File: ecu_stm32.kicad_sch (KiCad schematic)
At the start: 46 parts, among them J16 USB-C, J17 ARM Cortex Debug, Y2 16MHz

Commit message: Finished
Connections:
- net MEM1_nCS: now also U40.59 (PF11); no longer U40.50 (PA4)
- net RADIO1_DIO0 renamed ECU_GS
- new net ECU_BV: U40.50 (PA4)
- no-connect marks 73 -> 72
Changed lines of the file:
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@@
 	)
 	(no_connect
-		(at 193.04 96.52)
-	)
-	(no_connect
 		(at 162.56 86.36)
 	)
@@
 		)
 	)
+	(global_label "ECU_GS"
+		(shape input)
+		(at 193.04 76.2 0)
+		(fields_autoplaced yes)
+		(effects
+			(font
+				(size 1.27 1.27)
+			)
+			(justify left)
+		)
+		(property "Intersheetrefs" "${INTERSHEET_REFS}"
+			(at 203.2218 76.2 0)
+			(effects
+				(font
+					(size 1.27 1.27)
+				)
+				(justify left)
+				(hide yes)
+			)
+		)
+	)
 	(global_label "IMU_MOSI"
 		(shape input)
@@
 		)
 	)
+	(global_label "ECU_BV"
+		(shape input)
+		(at 162.56 30.48 180)
+		(fields_autoplaced yes)
+		(effects
+			(font
+				(size 1.27 1.27)
+			)
+			(justify right)
+		)
+		(property "Intersheetrefs" "${INTERSHEET_REFS}"
+			(at 152.4991 30.48 0)
+			(effects
+				(font
+					(size 1.27 1.27)
+				)
+				(justify right)
+				(hide yes)
+			)
+		)
+	)
 	(global_label "PT4"
 		(shape input)
@@
 		)
 	)
-	(global_label "RADIO1_DIO0"
-		(shape input)
-		(at 193.04 76.2 0)
-		(fields_autoplaced yes)
-		(effects
-			(font
-				(size 1.27 1.27)
-			)
-			(justify left)
-		)
-		(property "Intersheetrefs" "${INTERSHEET_REFS}"
-			(at 208.181 76.2 0)
-			(effects
-				(font
-					(size 1.27 1.27)
-				)
-				(justify left)
-				(hide yes)
-			)
-		)
-	)
 	(global_label "GPS_INT"
 		(shape input)
@@
 		)
 	)
-	(global_label "MEM1_nCS"
+	(global_label "GPS_TX"
 		(shape input)
-		(at 162.56 30.48 180)
+		(at 162.56 22.86 180)
 		(fields_autoplaced yes)
 		(effects
@@
 		)
 		(property "Intersheetrefs" "${INTERSHEET_REFS}"
-			(at 149.7174 30.48 0)
+			(at 152.6806 22.86 0)
 			(effects
 				(font
@@
 		)
 	)
-	(global_label "GPS_TX"
+	(global_label "RADIO_MISO"
 		(shape input)
-		(at 162.56 22.86 180)
+		(at 193.04 88.9 0)
 		(fields_autoplaced yes)
 		(effects
@@
 				(size 1.27 1.27)
 			)
-			(justify right)
+			(justify left)
 		)
 		(property "Intersheetrefs" "${INTERSHEET_REFS}"
-			(at 152.6806 22.86 0)
+			(at 207.0735 88.9 0)
 			(effects
 				(font
 					(size 1.27 1.27)
 				)
-				(justify right)
+				(justify left)
 				(hide yes)
 			)
 		)
 	)
-	(global_label "RADIO_MISO"
+	(global_label "MEM1_nCS"
 		(shape input)
-		(at 193.04 88.9 0)
+		(at 193.04 96.52 0)
 		(fields_autoplaced yes)
 		(effects
@@
 		)
 		(property "Intersheetrefs" "${INTERSHEET_REFS}"
-			(at 207.0735 88.9 0)
+			(at 205.8826 96.52 0)
 			(effects
 				(font

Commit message: Fully up to date
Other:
- note added: "IN IOC PH1 is OSC OUT"
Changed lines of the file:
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@@
+		)
+	)
+	(text "IN IOC PH1 is OSC OUT"
+		(exclude_from_sim no)
+		(at 255.016 64.262 0)
+		(effects
+			(font
+				(size 1.27 1.27)
+			)
 		)
 	)

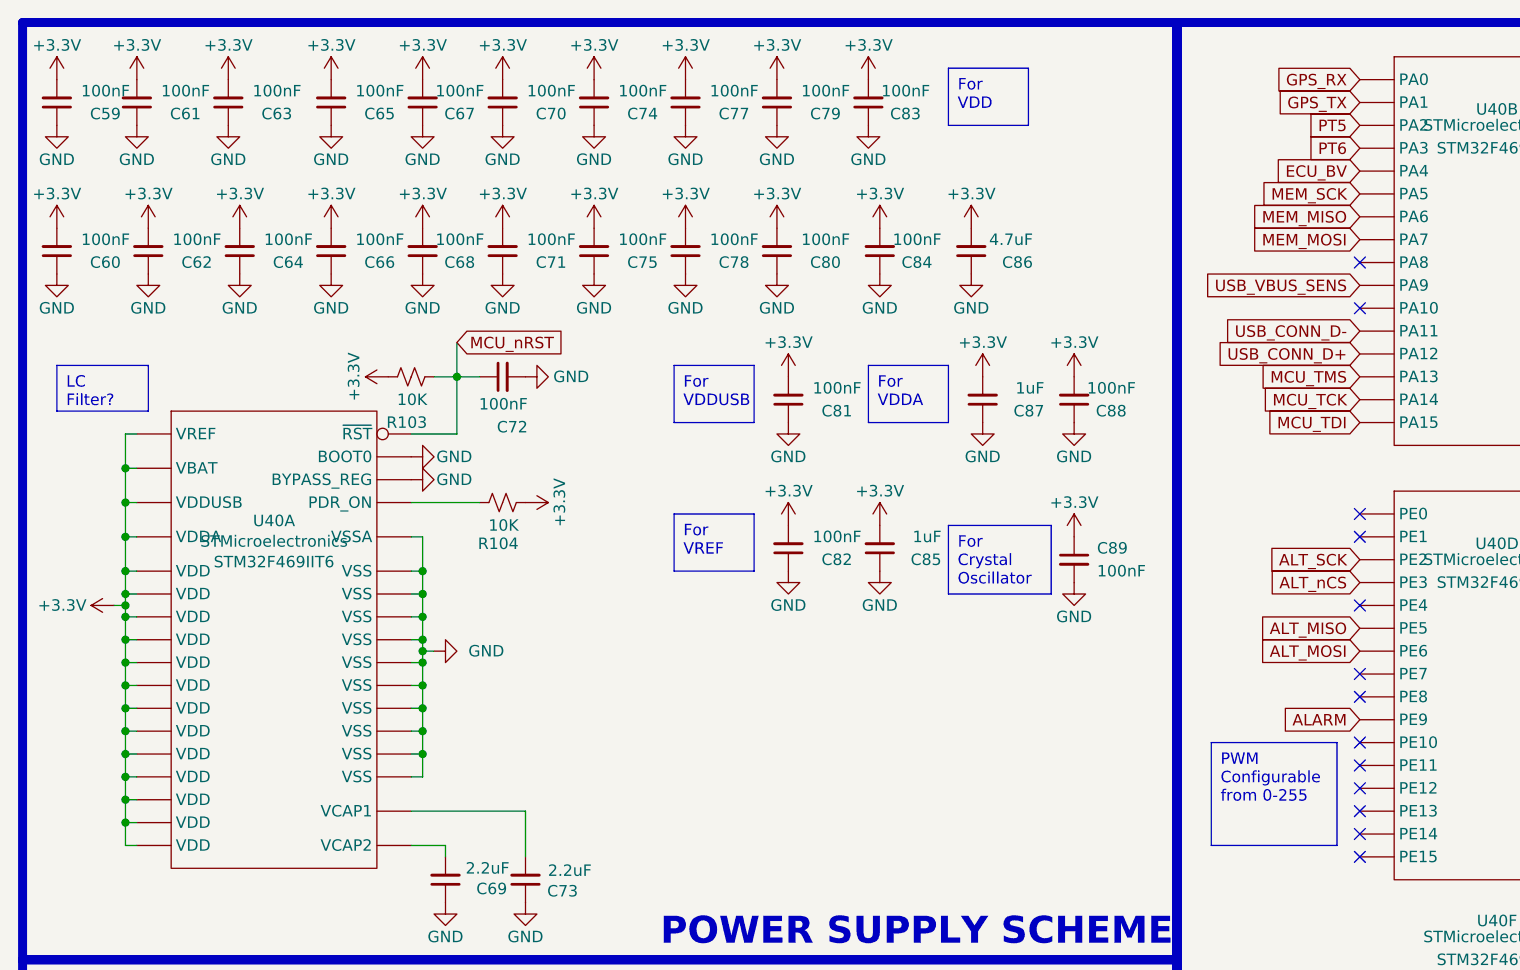
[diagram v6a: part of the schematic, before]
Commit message: REDS updated with diodes and hierarchy to main micro
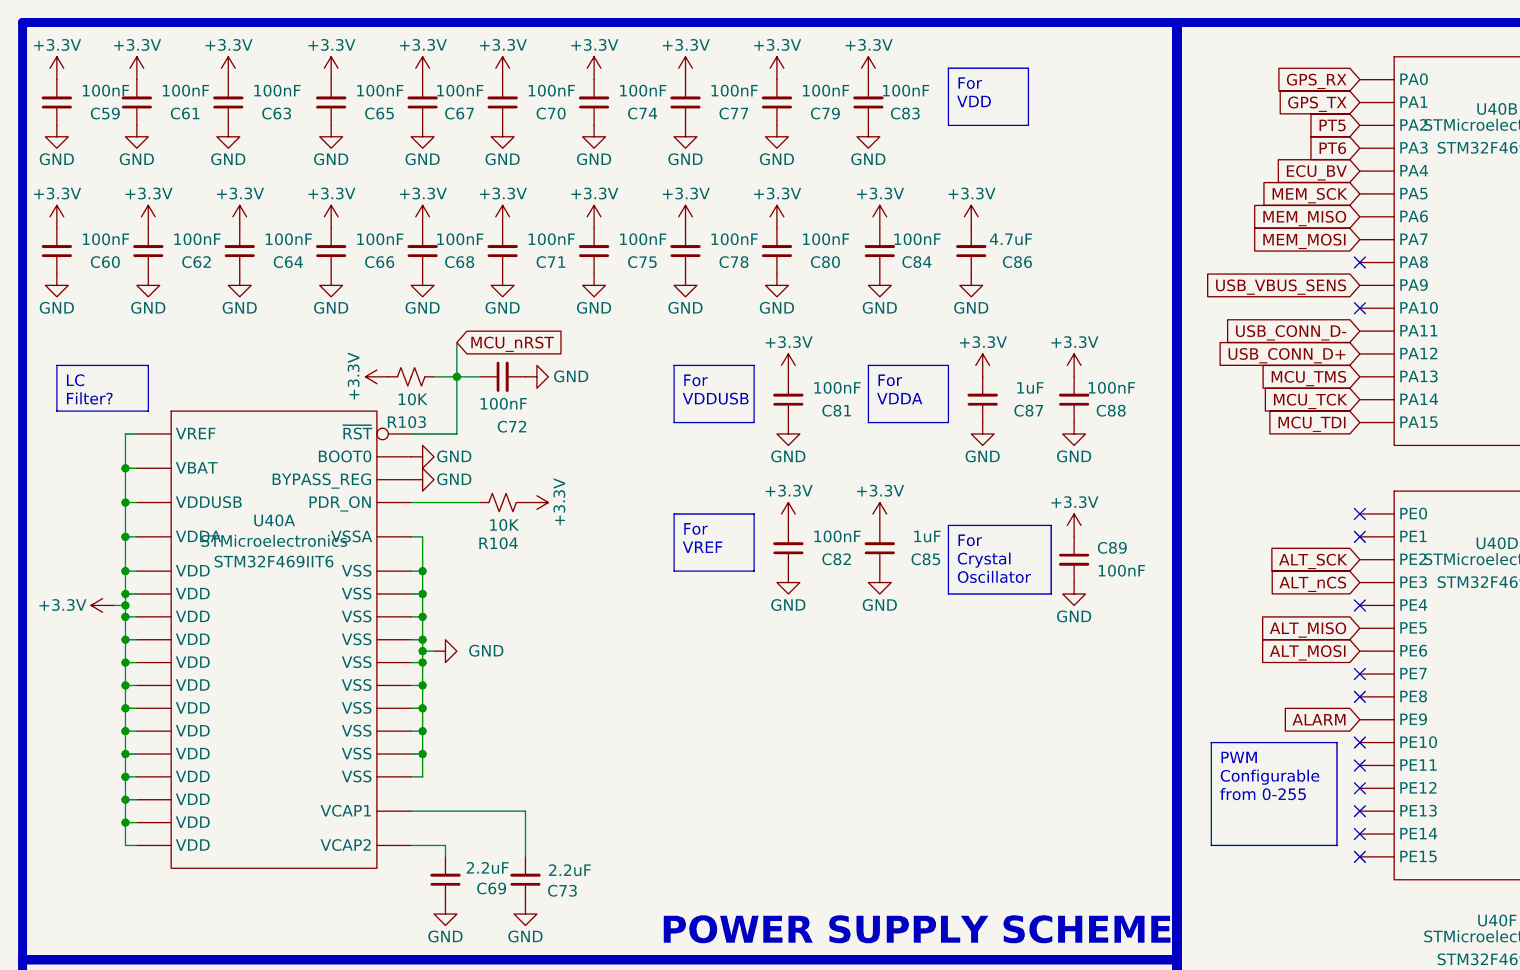
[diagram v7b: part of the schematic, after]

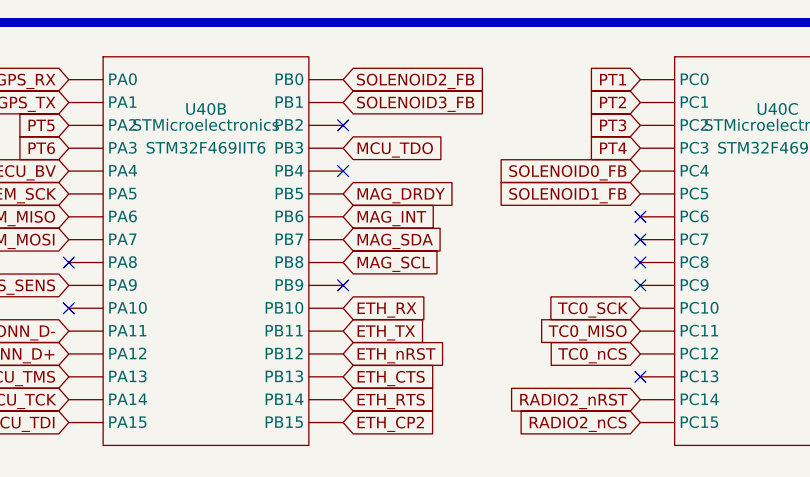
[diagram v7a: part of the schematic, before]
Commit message: moved from bmm150 to bmm350
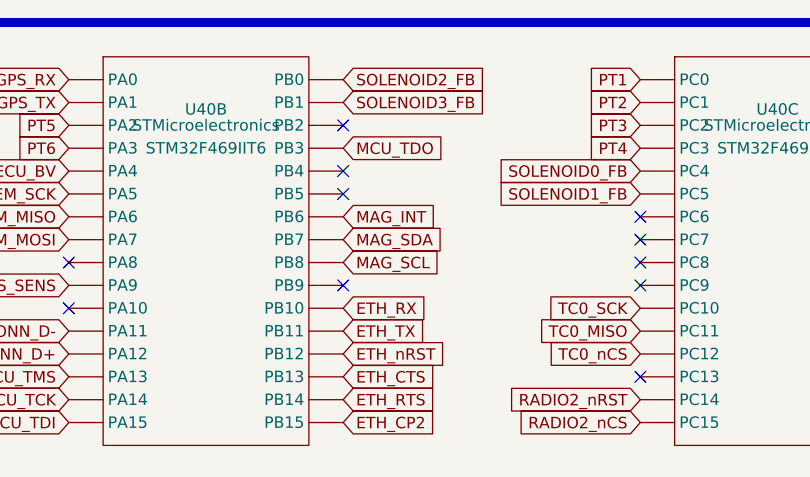
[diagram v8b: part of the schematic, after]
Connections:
- net MAG_DRDY: no longer names the net of U40.163 (PB5)
- no-connect marks 72 -> 73
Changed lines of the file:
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@@
+	)
+	(no_connect
+		(at 193.04 33.02)
 	)
 	(no_connect
@@
 				(hide yes)
 			)
-		)
-	)
-	(global_label "MAG_DRDY"
-		(shape input)
-		(at 193.04 33.02 0)
-		(fields_autoplaced yes)
-		(effects
-			(font
-				(size 1.27 1.27)
-			)
-			(justify left)
-		)
-		(property "Intersheetrefs" "${INTERSHEET_REFS}"
-			(at 205.622 33.02 0)
-			(effects
-				(font
-					(size 1.27 1.27)
-				)
-				(justify left)
-				(hide yes)
-			)
